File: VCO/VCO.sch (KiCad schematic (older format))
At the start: 104 parts, among them J1 SYNC, J10 SQR, J2 PWM, J3 LIN, J4 CV1, J5 CV2, J6 CV3, J7 SIN, J8 TRI, J9 RMP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

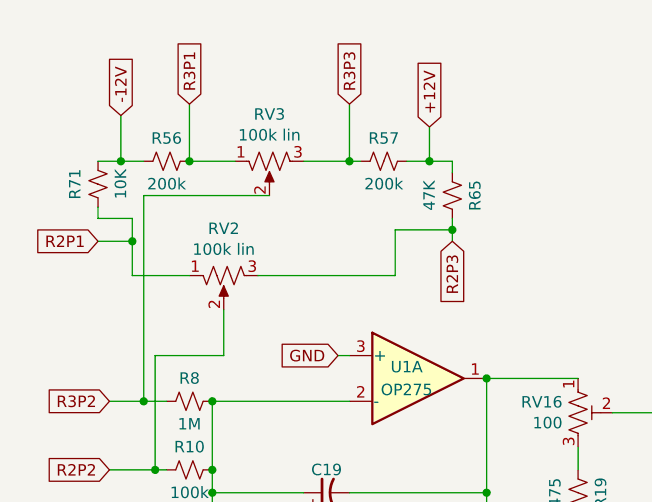
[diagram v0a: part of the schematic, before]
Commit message: Add files via upload
Fixed reversed pot leads and C12 silk polarity. Cleaned up some power routing.
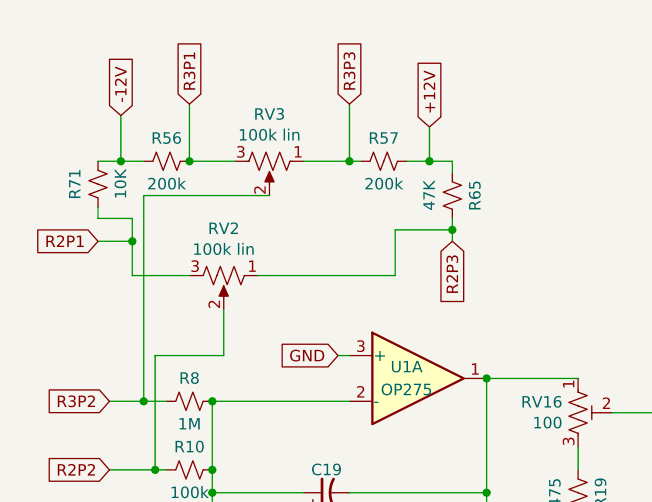
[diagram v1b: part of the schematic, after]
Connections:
- net R2P1: now also RV2.3; no longer RV2.1
- net R2P3: now also RV2.1; no longer RV2.3
- net R3P1: now also RV3.3; no longer RV3.1
- net R3P3: now also RV3.1; no longer RV3.3
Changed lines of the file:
@@
 F 3 "~" H 1300 1600 50  0001 C CNN
 	1    1300 1600
-	0    -1   1    0
+	0    1    1    0
 $EndComp
 Text GLabel 750  1450 0    50   Input ~ 0
@@
 F 3 "~" H 1500 1100 50  0001 C CNN
 	1    1500 1100
-	0    -1   1    0
-$EndComp
-Wire Wire Line
+	0    1    1    0
+$EndComp
+Wire Wire Line
